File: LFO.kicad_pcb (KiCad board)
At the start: 4 copper layers, 29.5 x 106.5 mm, 102 parts, among them J1 AudioJack2_SwitchT, J2 AudioJack2_SwitchT, J3 AudioJack2_SwitchT, J4 AudioJack2_SwitchT, J5 AudioJack2_SwitchT, J6 AudioJack2_SwitchT, J7 Conn_02x03_Odd_Even, J8 Conn_02x05_Odd_Even, Q1 BC847, SW1 SW_Push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

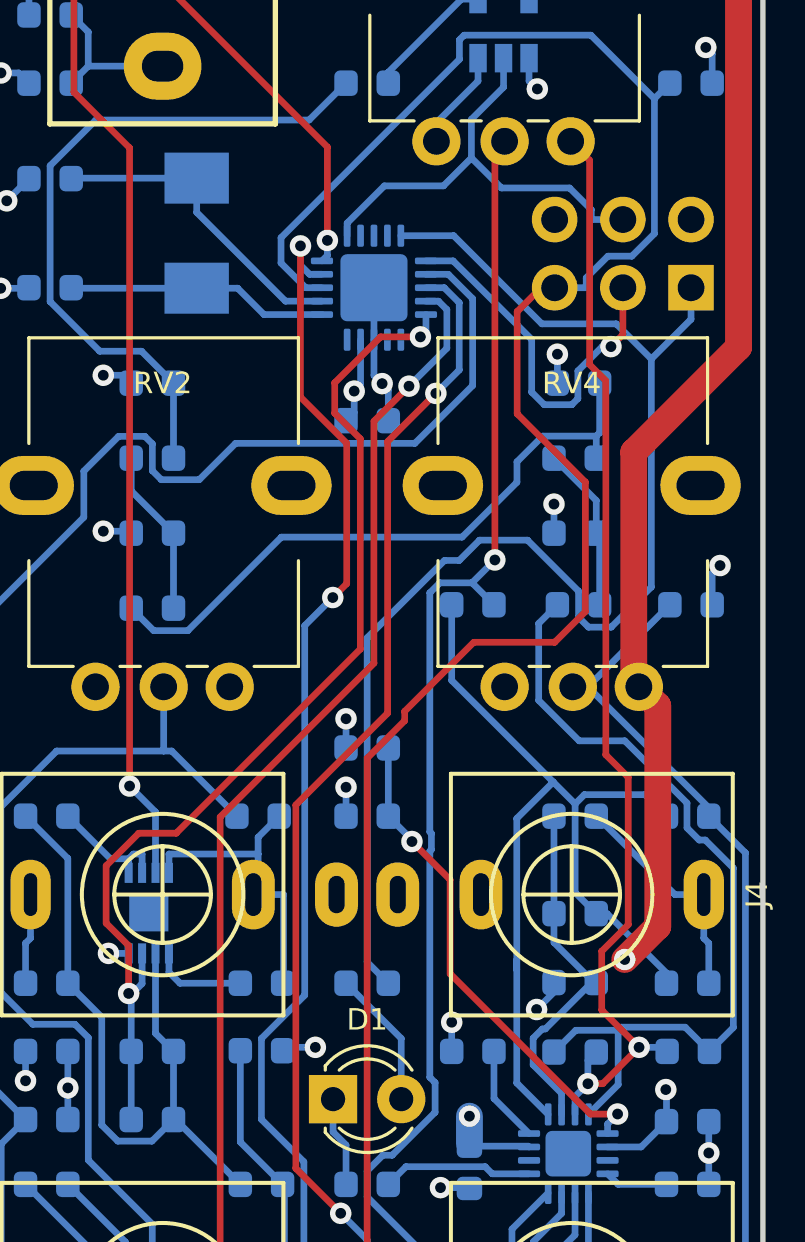
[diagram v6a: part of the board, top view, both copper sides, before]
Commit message: Moved a resistor for better routing.
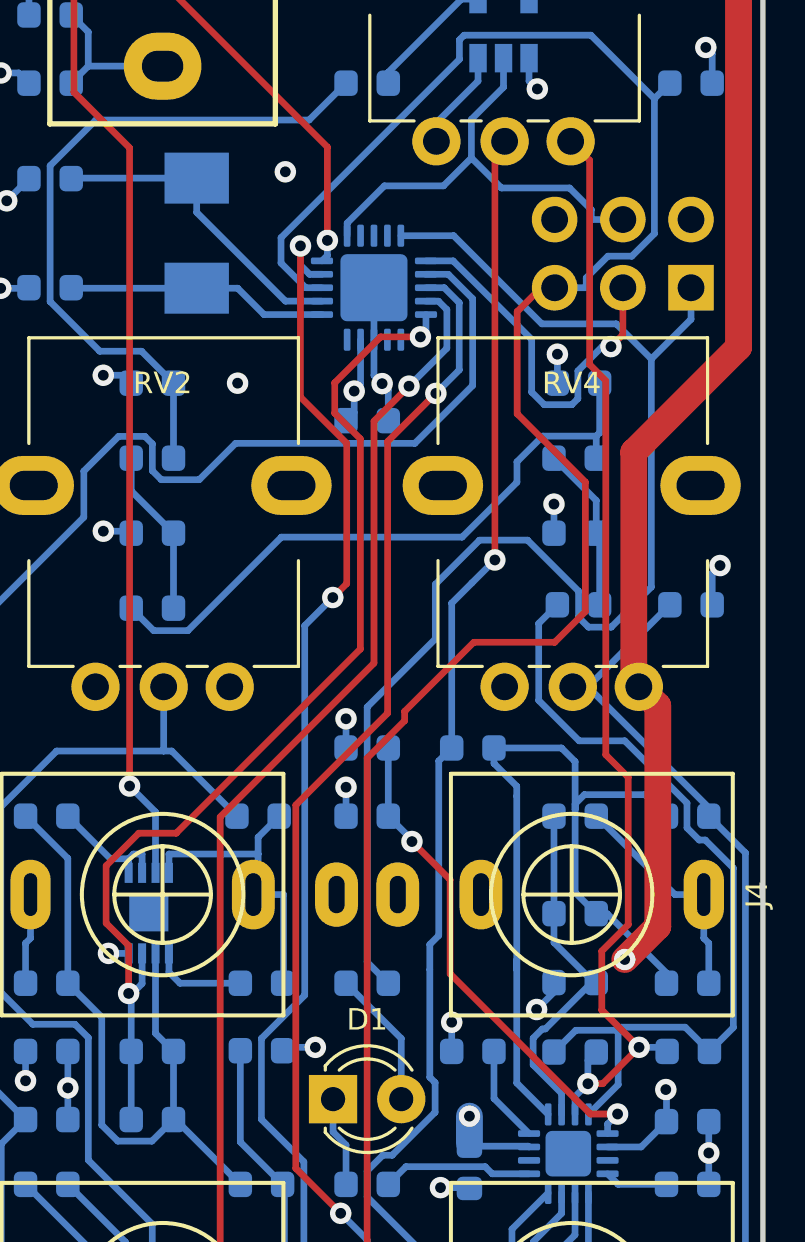
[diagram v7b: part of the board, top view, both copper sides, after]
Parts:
- moved R25 5.33 mm to (152.4, 114.8), turned to 0 degrees
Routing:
- net Net-(C16-Pad2): track 35.3 -> 32.1 mm
- net Net-(R25-Pad1): track 52.3 -> 50.4 mm
- net GND: vias 30 -> 32
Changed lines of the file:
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@@
     (thickness 1.6)
     (drawings 75)
-    (tracks 737)
+    (tracks 741)
     (zones 0)
     (modules 102)
@@
   )
   (module Resistor_SMD:R_0603_1608Metric (layer B.Cu)
-    (at 152.437 109.445 180)
+    (at 152.437 114.779)
     (descr "Resistor SMD 0603 (1608 Metric), square (rectangular) end terminal, IPC_7351 nominal, (Body size source: http://www.tortai-tech.com/upload/download/2011102023233369053.pdf), generated with kicad-footprint-generator")
     (tags resistor)
     (attr smd)
-    (fp_text reference R25 (at 0 -1.397 180) (layer B.SilkS)
+    (fp_text reference R25 (at 0 -1.397) (layer B.SilkS)
       (effects (font (size 0.8 0.8) (thickness 0.15)) (justify mirror))
     )
-    (fp_text value 100k (at 0 -1.43 180) (layer B.Fab)
+    (fp_text value 100k (at 0 -1.43) (layer B.Fab)
       (effects (font (size 1 1) (thickness 0.15)) (justify mirror))
     )
-    (fp_text user %R (at 0 0 180) (layer B.Fab)
+    (fp_text user %R (at 0 0) (layer B.Fab)
       (effects (font (size 1 1) (thickness 0.15)) (justify mirror))
     )
@@
     (fp_line (start -0.8 0.4) (end 0.8 0.4) (layer B.Fab) (width 0.1))
     (fp_line (start -0.8 -0.4) (end -0.8 0.4) (layer B.Fab) (width 0.1))
-    (pad 2 smd roundrect (at 0.7875 0 180) (size 0.875 0.95) (layers B.Cu B.Paste B.Mask) (roundrect_rratio 0.25)
+    (pad 2 smd roundrect (at 0.7875 0) (size 0.875 0.95) (layers B.Cu B.Paste B.Mask) (roundrect_rratio 0.25)
       (net 19 "Net-(C16-Pad2)"))
-    (pad 1 smd roundrect (at -0.7875 0 180) (size 0.875 0.95) (layers B.Cu B.Paste B.Mask) (roundrect_rratio 0.25)
+    (pad 1 smd roundrect (at -0.7875 0) (size 0.875 0.95) (layers B.Cu B.Paste B.Mask) (roundrect_rratio 0.25)
       (net 18 "Net-(R25-Pad1)"))
     (model ${KISYS3DMOD}/Resistor_SMD.3dshapes/R_0603_1608Metric.wrl
@@
   (segment (start 159.0859 100.2884) (end 160.565 98.8093) (width 0.25) (layer B.Cu) (net 9))
   (segment (start 160.565 97.634) (end 160.565 98.8093) (width 0.25) (layer B.Cu) (net 9))
-  (segment (start 159.0859 108.7836) (end 159.0859 100.2884) (width 0.25) (layer B.Cu) (net 9))
   (segment (start 157.5914 110.2781) (end 159.0859 108.7836) (width 0.25) (layer B.Cu) (net 9))
   (segment (start 156.7444 110.2781) (end 157.5914 110.2781) (width 0.25) (layer B.Cu) (net 9))
+  (segment (start 156.374 109.9077) (end 156.7444 110.2781) (width 0.25) (layer B.Cu) (net 9))
   (segment (start 156.374 108.9371) (end 156.374 109.9077) (width 0.25) (layer B.Cu) (net 9))
-  (segment (start 148.5 122.7545) (end 148.5 110.6752) (width 0.25) (layer B.Cu) (net 9))
-  (segment (start 152.6861 107.0369) (end 154.4738 107.0369) (width 0.25) (layer B.Cu) (net 9))
-  (segment (start 154.4738 107.0369) (end 156.374 108.9371) (width 0.25) (layer B.Cu) (net 9))
+  (segment (start 159.0859 108.7836) (end 159.0859 100.2884) (width 0.25) (layer B.Cu) (net 9))
   (segment (start 149.2875 123.542) (end 148.5 122.7545) (width 0.25) (layer B.Cu) (net 9))
-  (segment (start 156.374 109.9077) (end 156.7444 110.2781) (width 0.25) (layer B.Cu) (net 9))
-  (segment (start 148.5 110.6752) (end 151.3812 107.794) (width 0.25) (layer B.Cu) (net 9))
-  (segment (start 151.3812 107.794) (end 151.929 107.794) (width 0.25) (layer B.Cu) (net 9))
-  (segment (start 151.929 107.794) (end 152.6861 107.0369) (width 0.25) (layer B.Cu) (net 9))
+  (segment (start 148.5 122.7545) (end 148.5 113.255) (width 0.25) (layer B.Cu) (net 9))
+  (segment (start 154.4738 107.0369) (end 156.374 108.9371) (width 0.25) (layer B.Cu) (net 9))
+  (segment (start 148.5 113.255) (end 151.04 110.715) (width 0.25) (layer B.Cu) (net 9))
+  (segment (start 151.04 110.715) (end 151.04 108.683) (width 0.25) (layer B.Cu) (net 9))
+  (segment (start 151.04 108.683) (end 152.6861 107.0369) (width 0.25) (layer B.Cu) (net 9))
+  (segment (start 152.6861 107.0369) (end 154.4738 107.0369) (width 0.25) (layer B.Cu) (net 9))
   (segment (start 149.77 127.86) (end 149.77 125.5995) (width 0.25) (layer B.Cu) (net 10))
   (segment (start 149.77 125.5995) (end 147.7125 123.542) (width 0.25) (layer B.Cu) (net 10))
@@
   (segment (start 153.62 92.18) (end 153.2576 92.5424) (width 0.25) (layer F.Cu) (net 18))
   (segment (start 153.2576 92.5424) (end 153.2576 107.7755) (width 0.25) (layer F.Cu) (net 18))
-  (segment (start 152.4063 108.6268) (end 153.2576 107.7755) (width 0.25) (layer B.Cu) (net 18))
-  (segment (start 152.4063 108.6268) (end 153.2245 109.445) (width 0.25) (layer B.Cu) (net 18))
   (segment (start 151.6495 138.782) (end 151.14 138.2725) (width 0.25) (layer B.Cu) (net 18))
   (segment (start 151.14 138.2725) (end 151.14 134.1443) (width 0.25) (layer B.Cu) (net 18))
@@
   (segment (start 151.0308 128.3509) (end 151.0308 127.243) (width 0.25) (layer B.Cu) (net 18))
   (segment (start 151.0308 127.243) (end 150.8337 127.0459) (width 0.25) (layer B.Cu) (net 18))
-  (segment (start 150.8337 127.0459) (end 150.8337 118.6255) (width 0.25) (layer B.Cu) (net 18))
-  (segment (start 150.8337 118.6255) (end 150.8939 118.5653) (width 0.25) (layer B.Cu) (net 18))
-  (segment (start 150.8939 118.5653) (end 150.8939 117.9643) (width 0.25) (layer B.Cu) (net 18))
-  (segment (start 150.8939 117.9643) (end 150.8337 117.9041) (width 0.25) (layer B.Cu) (net 18))
-  (segment (start 150.8337 117.9041) (end 150.8337 109.0001) (width 0.25) (layer B.Cu) (net 18))
-  (segment (start 150.8337 109.0001) (end 151.207 108.6268) (width 0.25) (layer B.Cu) (net 18))
-  (segment (start 151.207 108.6268) (end 152.4063 108.6268) (width 0.25) (layer B.Cu) (net 18))
   (via (at 153.2576 107.7755) (size 0.8) (layers F.Cu B.Cu) (net 18))
-  (segment (start 155.4318 116.0467) (end 151.6495 112.2644) (width 0.25) (layer B.Cu) (net 19))
-  (segment (start 151.6495 112.2644) (end 151.6495 109.445) (width 0.25) (layer B.Cu) (net 19))
-  (segment (start 156.247 116.8619) (end 155.4318 116.0467) (width 0.25) (layer B.Cu) (net 19))
+  (segment (start 150.8337 123.034) (end 150.8337 122.0973) (width 0.25) (layer B.Cu) (net 18))
+  (segment (start 150.8337 127.0459) (end 150.8337 123.034) (width 0.25) (layer B.Cu) (net 18))
+  (segment (start 150.8337 122.0973) (end 151.167 121.764) (width 0.25) (layer B.Cu) (net 18))
+  (segment (start 151.167 115.2615) (end 151.6495 114.779) (width 0.25) (layer B.Cu) (net 18))
+  (segment (start 151.167 121.764) (end 151.167 115.2615) (width 0.25) (layer B.Cu) (net 18))
+  (segment (start 152.4063 108.6268) (end 153.2576 107.7755) (width 0.25) (layer B.Cu) (net 18))
+  (segment (start 151.6495 114.779) (end 151.6495 109.3836) (width 0.25) (layer B.Cu) (net 18))
+  (segment (start 151.6495 109.3836) (end 152.4063 108.6268) (width 0.25) (layer B.Cu) (net 18))
   (segment (start 157.0345 120.951) (end 157.4385 120.951) (width 0.25) (layer B.Cu) (net 19))
   (segment (start 157.4385 120.951) (end 159.6505 123.163) (width 0.25) (layer B.Cu) (net 19))
@@
   (segment (start 158.8493 116.5178) (end 159.6505 117.319) (width 0.25) (layer B.Cu) (net 19))
   (segment (start 157.0345 120.951) (end 156.247 120.1635) (width 0.25) (layer B.Cu) (net 19))
-  (segment (start 156.247 120.1635) (end 156.247 116.8619) (width 0.25) (layer B.Cu) (net 19))
-  (segment (start 154.0726 117.4059) (end 154.0726 123.034) (width 0.25) (layer B.Cu) (net 19))
   (segment (start 154.0726 123.034) (end 154.0726 122.6684) (width 0.25) (layer B.Cu) (net 19))
-  (segment (start 155.4318 116.0467) (end 154.0726 117.4059) (width 0.25) (layer B.Cu) (net 19))
   (segment (start 154.0726 127.2591) (end 155.243 128.4295) (width 0.25) (layer B.Cu) (net 19))
   (segment (start 154.0726 123.034) (end 154.0726 127.2591) (width 0.25) (layer B.Cu) (net 19))
+  (segment (start 154.0726 116.5724) (end 154.0726 123.034) (width 0.25) (layer B.Cu) (net 19))
+  (segment (start 154.0726 116.2021) (end 154.0726 116.5724) (width 0.25) (layer B.Cu) (net 19))
+  (segment (start 153.2245 115.354) (end 154.0726 116.2021) (width 0.25) (layer B.Cu) (net 19))
+  (segment (start 153.2245 114.779) (end 153.2245 115.354) (width 0.25) (layer B.Cu) (net 19))
+  (segment (start 155.738494 114.779) (end 156.247 115.287506) (width 0.25) (layer B.Cu) (net 19))
+  (segment (start 153.2245 114.779) (end 155.738494 114.779) (width 0.25) (layer B.Cu) (net 19))
+  (segment (start 156.247 120.1635) (end 156.247 117.065) (width 0.25) (layer B.Cu) (net 19))
+  (segment (start 156.247 115.287506) (end 156.247 117.065) (width 0.25) (layer B.Cu) (net 19))
+  (segment (start 156.247 117.065) (end 156.247 116.8619) (width 0.25) (layer B.Cu) (net 19))
   (segment (start 157.0345 106.778) (end 157.0345 105.559) (width 0.25) (layer B.Cu) (net 20))
   (segment (start 157.0345 105.559) (end 155.4595 103.984) (width 0.25) (layer B.Cu) (net 20))
@@
   (via (at 139.268 74.0605) (size 0.8) (layers F.Cu B.Cu) (net 65))
   (via (at 159.295 60.8895) (size 0.8) (layers F.Cu B.Cu) (net 65))
+  (via (at 145.452 93.316) (size 0.8) (drill 0.4) (layers F.Cu B.Cu) (net 65))
+  (via (at 143.674 101.19) (size 0.8) (drill 0.4) (layers F.Cu B.Cu) (net 65))
   (segment (start 159.6505 141.322) (end 159.6505 138.832) (width 0.25) (layer B.Cu) (net 66))
   (segment (start 159.6505 138.832) (end 159.6255 138.807) (width 0.25) (layer B.Cu) (net 66))
